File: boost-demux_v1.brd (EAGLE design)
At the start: 83.8 x 57.1 mm, 45 parts, among them M1 6-32_MOUNT, M2 6-32_MOUNT, M3 6-32_MOUNT, M4 6-32_MOUNT, Q1 ON_FDD4141, U1 TI_TPS55330, U2 4067D, U5 AVAGO_ACPL-217

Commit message: Added minor PCB markup
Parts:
- D2: value GREEN -> +5V
- D3: value GREEN -> +12V
- D4: value GREEN -> +20V
- D5: value RED -> ENABLE
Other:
- board text added: "HP C6602A CONTROLLER V1.0"
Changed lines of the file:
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@@
 <text x="7.62" y="11.43" size="2.54" layer="21" font="vector" ratio="10" rot="R90" align="top-center">EN</text>
 <text x="2.54" y="45.72" size="2.54" layer="21" font="vector" ratio="10" rot="R90" align="center-left">+</text>
+<text x="26.67" y="49.022" size="1.905" layer="21" font="vector" ratio="10" align="bottom-center">HP C6602A
+CONTROLLER V1.0</text>
 </plain>
 <attributes>
@@
 </element>
 <element name="D1" library="components" package="TO-277-3" value="ON_FSV8100V" x="33.02" y="30.48" rot="R180"/>
-<element name="D2" library="SparkFun-LED" package="LED_5MM" value="GREEN" x="60.96" y="50.8"/>
-<element name="D3" library="SparkFun-LED" package="LED_5MM" value="GREEN" x="66.04" y="43.18"/>
-<element name="D4" library="SparkFun-LED" package="LED_5MM" value="GREEN" x="71.12" y="50.8"/>
-<element name="D5" library="SparkFun-LED" package="LED_5MM" value="RED" x="76.2" y="43.18"/>
+<element name="D2" library="SparkFun-LED" package="LED_5MM" value="+5V" x="60.96" y="50.8" smashed="yes">
+<attribute name="NAME" x="60.96" y="54.1909" size="1.27" layer="25" font="vector" ratio="10" align="bottom-center"/>
+<attribute name="VALUE" x="60.9854" y="47.4091" size="1.27" layer="27" font="vector" ratio="10" align="top-center"/>
+</element>
+<element name="D3" library="SparkFun-LED" package="LED_5MM" value="+12V" x="66.04" y="43.18" smashed="yes">
+<attribute name="NAME" x="66.04" y="46.5709" size="1.27" layer="25" font="vector" ratio="10" align="bottom-center"/>
+<attribute name="VALUE" x="66.0654" y="39.7891" size="1.27" layer="27" font="vector" ratio="10" align="top-center"/>
+</element>
+<element name="D4" library="SparkFun-LED" package="LED_5MM" value="+20V" x="71.12" y="50.8" smashed="yes">
+<attribute name="NAME" x="71.12" y="54.1909" size="1.27" layer="25" font="vector" ratio="10" align="bottom-center"/>
+<attribute name="VALUE" x="71.1454" y="47.4091" size="1.27" layer="27" font="vector" ratio="10" align="top-center"/>
+</element>
+<element name="D5" library="SparkFun-LED" package="LED_5MM" value="ENABLE" x="76.2" y="43.18" smashed="yes">
+<attribute name="NAME" x="76.2" y="46.5709" size="1.27" layer="25" font="vector" ratio="10" align="bottom-center"/>
+<attribute name="VALUE" x="76.2254" y="39.7891" size="1.27" layer="27" font="vector" ratio="10" align="top-center"/>
+</element>
 <element name="D6" library="components" package="TO-277-3" value="ON_FSV8100V" x="59.69" y="36.83" rot="R180"/>
 <element name="L1" library="components" package="4440" value="4.7U" x="33.02" y="41.91" smashed="yes" rot="R270">
@@
 <wire x1="53.34" y1="3.81" x2="53.34" y2="13.208" width="0.6096" layer="1"/>
 <wire x1="53.34" y1="13.208" x2="54.61" y2="14.478" width="0.6096" layer="1"/>
-<wire x1="54.61" y1="14.478" x2="64.008" y2="14.478" width="0.6096" layer="1"/>
-<wire x1="64.008" y1="14.478" x2="64.77" y2="15.24" width="0.6096" layer="1"/>
-<wire x1="64.77" y1="15.24" x2="64.77" y2="20.574" width="0.6096" layer="1"/>
+<wire x1="54.61" y1="14.478" x2="63.754" y2="14.478" width="0.6096" layer="1"/>
+<wire x1="63.754" y1="14.478" x2="64.77" y2="15.494" width="0.6096" layer="1"/>
+<wire x1="64.77" y1="15.494" x2="64.77" y2="20.574" width="0.6096" layer="1"/>
 <wire x1="78.74" y1="26.67" x2="77.47" y2="27.94" width="0.6096" layer="1"/>
 <wire x1="77.47" y1="27.94" x2="73.66" y2="27.94" width="0.6096" layer="1"/>
@@
 </drawing>
 <compatibility>
+<note version="6.3" minversion="6.2.2" severity="warning">
+Since Version 6.2.2 text objects can contain more than one line,
+which will not be processed correctly with this version.
+</note>
 <note version="8.2" severity="warning">
 Since Version 8.2, EAGLE supports online libraries. The ids

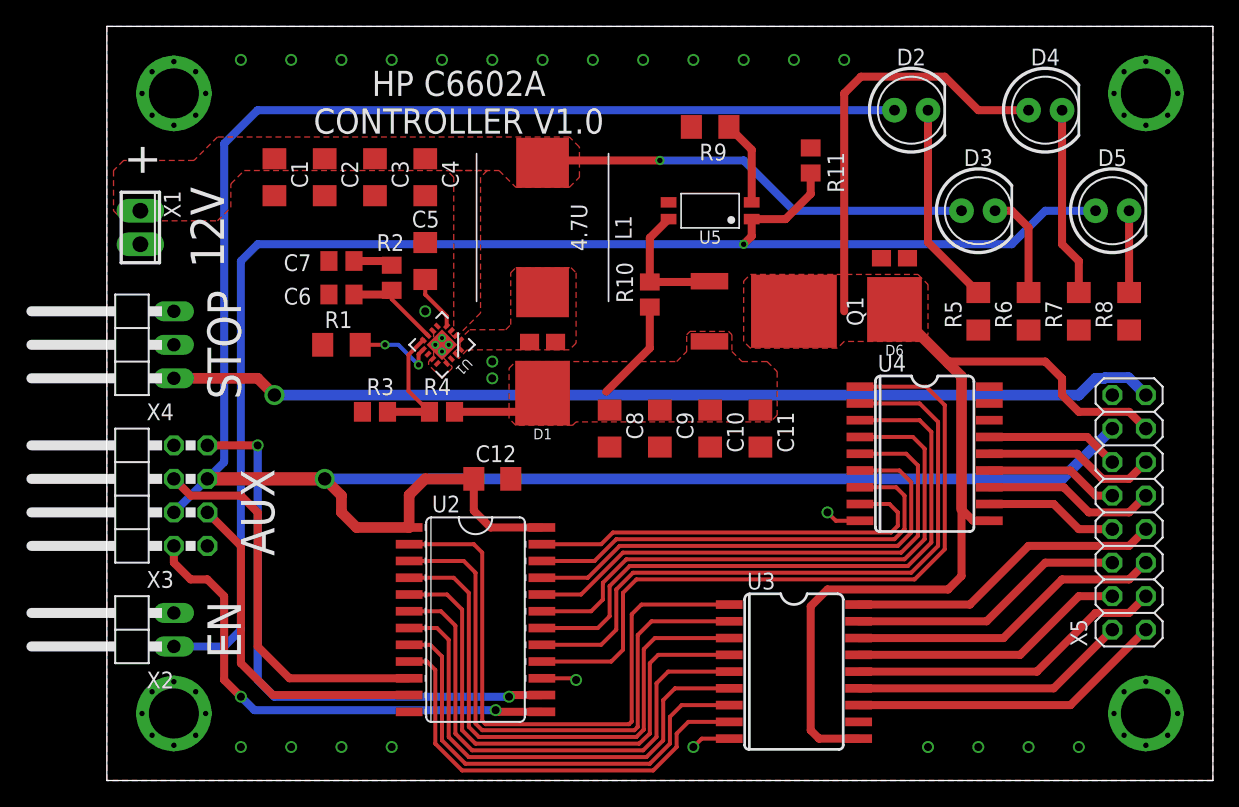
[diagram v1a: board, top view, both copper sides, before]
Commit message: Updates to boost-demux and FFC breakout
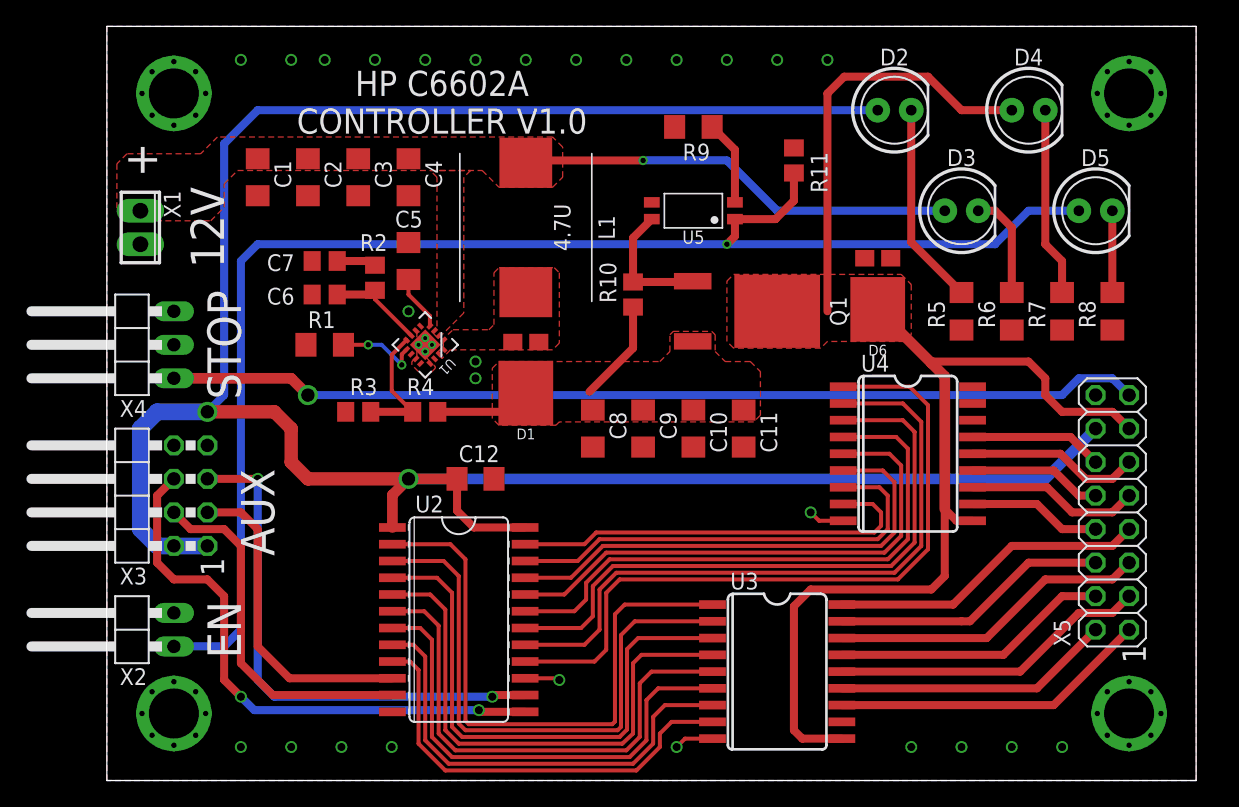
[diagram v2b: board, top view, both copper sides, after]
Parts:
- moved D3 1.27 mm to (64.8, 43.2)
- moved D4 1.27 mm to (69.8, 50.8)
- moved R5 1.27 mm to (64.8, 35.6)
- moved C11 1.27 mm to (48.3, 26.7)
- moved C8 1.27 mm to (36.8, 26.7)
- moved D1 1.27 mm to (31.8, 30.5)
- moved D2 1.27 mm to (59.7, 50.8)
- moved L1 1.27 mm to (31.8, 41.9)
- moved Q1 1.27 mm to (50.8, 35.6)
- moved R10 1.27 mm to (39.9, 36.8)
- moved R11 1.27 mm to (52.1, 47.0)
- moved U3 1.27 mm to (50.8, 12.7)
- moved C2 1.27 mm to (15.2, 45.7)
- moved C1 1.27 mm to (11.4, 45.7)
- moved C12 1.27 mm to (27.9, 22.9)
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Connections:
- net +5V: now also X3.1, X3.2; no longer X3.4, X3.5
- net A: now also X3.3; no longer X3.6
- net B: now also X3.4; no longer X3.3
- net C: now also X3.5; no longer X3.7
- net D: now also X3.6; no longer X3.2
- net GND: now also X3.7; no longer X3.1, X4.3
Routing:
- net D: track 37.6 -> 43.2 mm
- net A: track 30.0 -> 24.4 mm
- net C: track 43.7 -> 39.9 mm
- net +5V: track 176.2 -> 178.7 mm, vias 1 -> 2
- net STOP: track 75.3 -> 74.0 mm
- net B: track 26.2 -> 27.5 mm
- net EN: track 108.9 -> 107.9 mm
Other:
- board size 83.8 x 57.1 mm -> 82.5 x 57.1 mm
- board text added: "1"

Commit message: Logos
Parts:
- added LOGO1: MADOG, components:MADOG
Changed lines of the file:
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@@
 <element name="M3" library="components" package="6-32_MOUNT" value="6-32_MOUNT" x="77.47" y="52.07"/>
 <element name="M4" library="components" package="6-32_MOUNT" value="6-32_MOUNT" x="77.47" y="5.08"/>
+<element name="LOGO1" library="components" package="MADOG" value="MADOG" x="16.51" y="14.732"/>
 </elements>
 <signals>
